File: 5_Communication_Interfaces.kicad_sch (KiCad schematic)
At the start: 26 parts, among them J50 I2C_EXP, J51 UART2_DEBUG, J53 NRF24_PA_LNA, J56 Screw_Terminal_01x03, U10 TJA1051T-3

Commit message: Updated BOM. Initial review and corrections
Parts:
- C60, C61: LCSC C1632 -> C14858
- C62, J50, J51, J53, J56, JP1, U10: now left out of the parts list
- C63: value 10uF -> 10uF/25V; LCSC C13585 -> C6119815
- C64, C70, C71, C72, C74: value 0.1uF -> 100nF/50V; LCSC C1848 -> C6119867
- FB50: LCSC C1015 -> C16902
- R60, R61: LCSC C17936 -> C23162
- R62, R63: LCSC C17901 -> C22775
- R66, R67, R68, R69: LCSC C25117 -> C1211
- R75: LCSC C17909 -> C114640

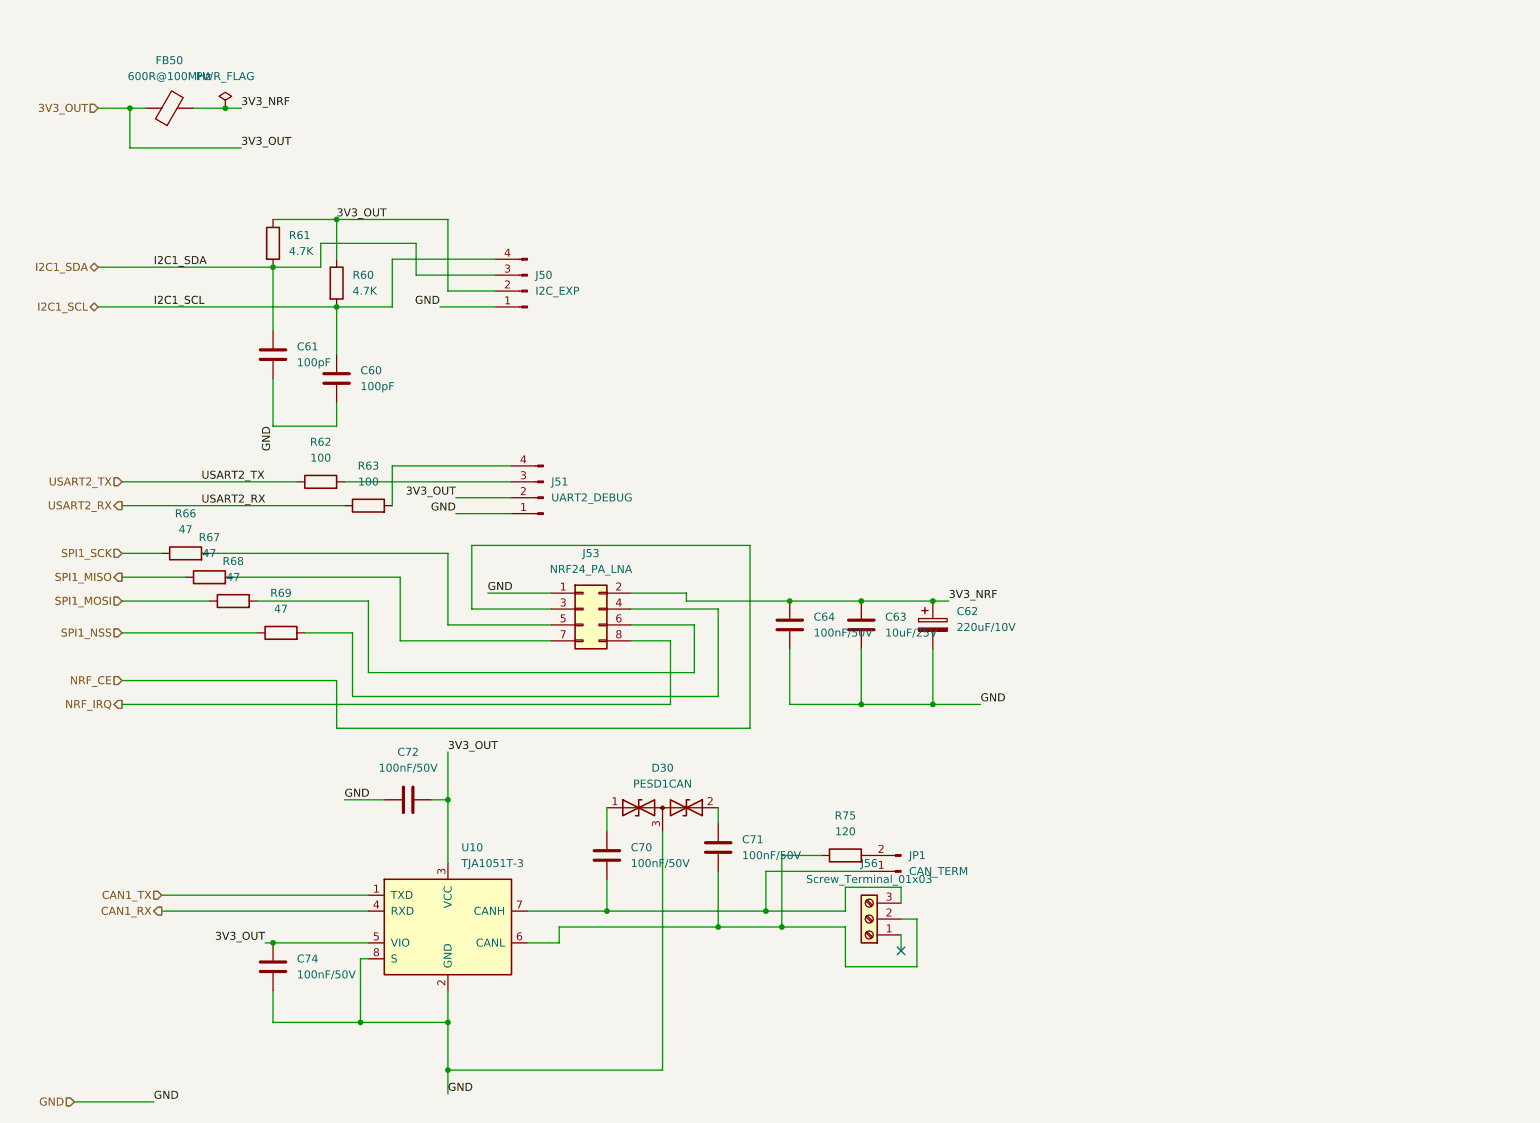
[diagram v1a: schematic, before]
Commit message: Cleaned up schematic. Added mounting holes.
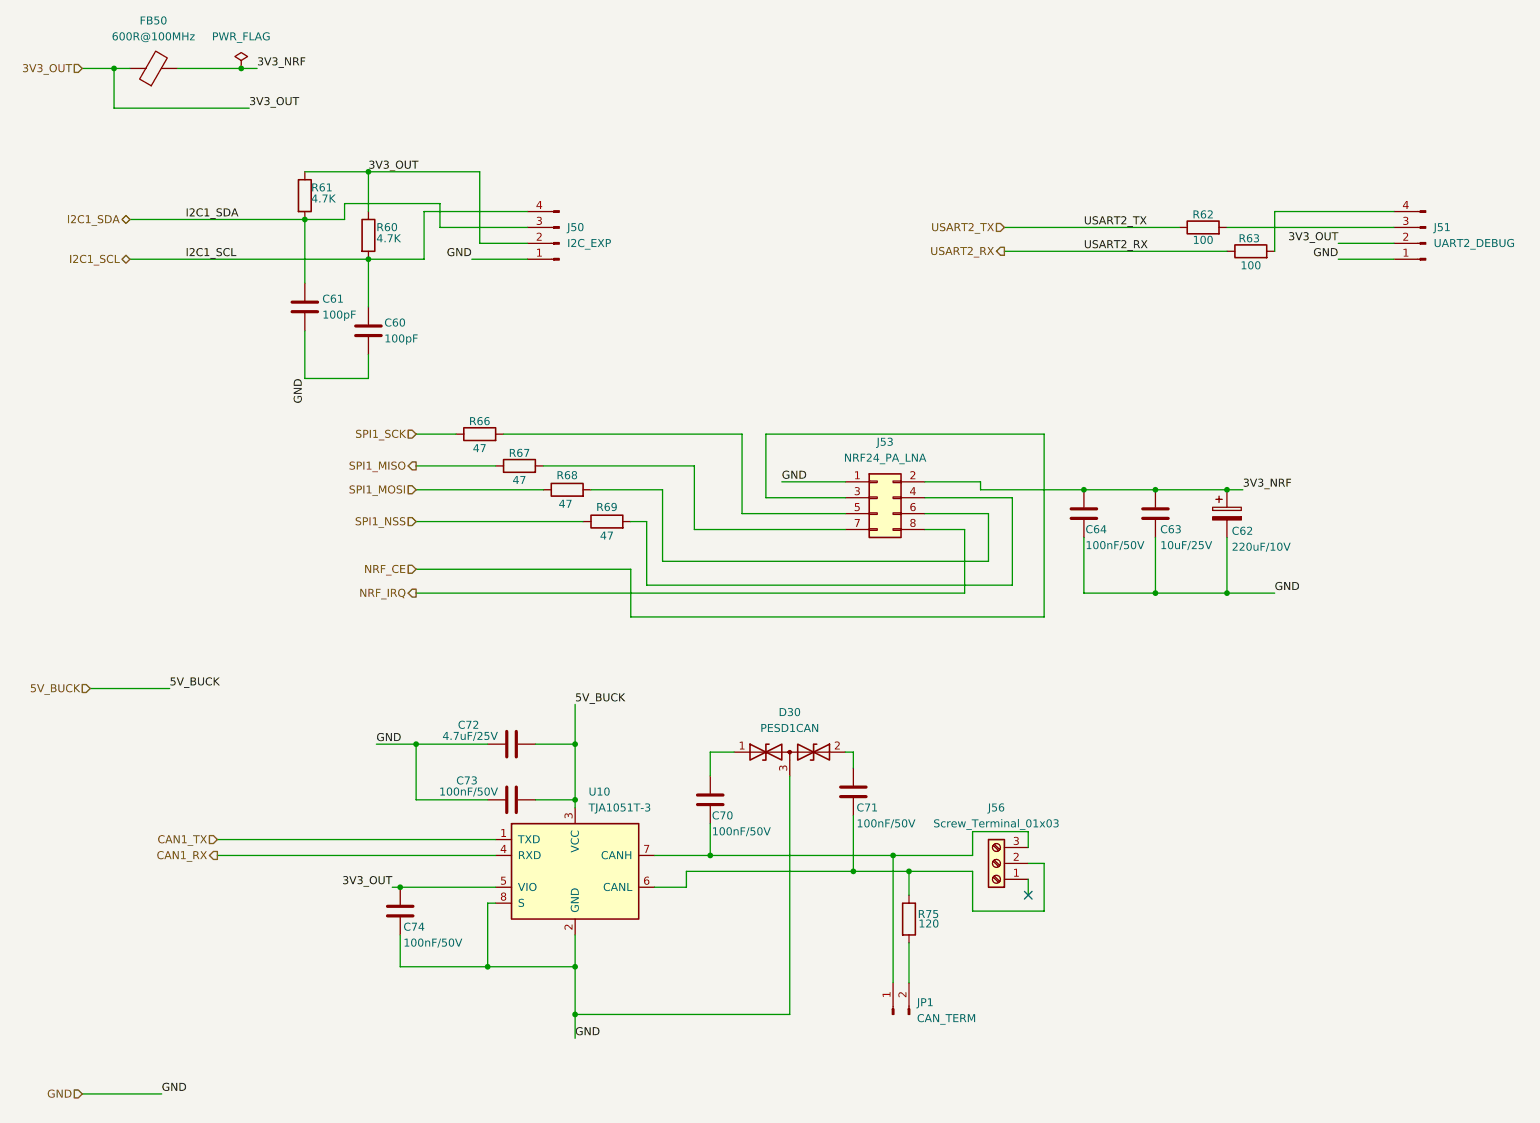
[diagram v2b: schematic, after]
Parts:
- added C72: 4.7uF/25V, Capacitor_SMD:C_0603_1608Metric, symbol Device:C
- renumbered C72 to C73
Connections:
- net 3V3_OUT: no longer C73.1, U10.3 (VCC)
- net GND: now also C72.1
- new net 5V_BUCK: C72.2, C73.1, U10.3 (VCC)
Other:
- moved on the sheet: C60, C61, C62, C63, C64, C70, C71, C73, C74, D30, FB50, J50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
